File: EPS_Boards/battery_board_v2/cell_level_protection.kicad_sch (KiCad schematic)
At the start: 31 parts

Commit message: eps: battery board: updated schematic
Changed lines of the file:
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@@
     )
   )
-  (global_label "LOW_SIDE_INHIBIT" (shape input) (at 161.29 166.37 180) (fields_autoplaced)
+  (global_label "PACK_N" (shape input) (at 161.29 166.37 180) (fields_autoplaced)
     (effects (font (size 1.27 1.27)) (justify right))
-    (property "Intersheet References" "${INTERSHEET_REFS}" (id 0) (at 142.1855 166.2906 0)
+    (property "Intersheet References" "${INTERSHEET_REFS}" (id 0) (at 151.6802 166.2906 0)
       (effects (font (size 1.27 1.27)) (justify right) hide)
     )
@@
     )
   )
+  (global_label "PACK_P" (shape input) (at 168.91 43.18 270) (fields_autoplaced)
+    (effects (font (size 1.27 1.27)) (justify right))
+    (property "Intersheet References" "${INTERSHEET_REFS}" (id 0) (at 168.9894 52.7293 90)
+      (effects (font (size 1.27 1.27)) (justify right) hide)
+    )
+  )

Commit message: eps: battery board: fixed errors
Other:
- note added: "IV monitor here"
- moved on the sheet: BT?, C?, F?, J?, Q?, R?, U?

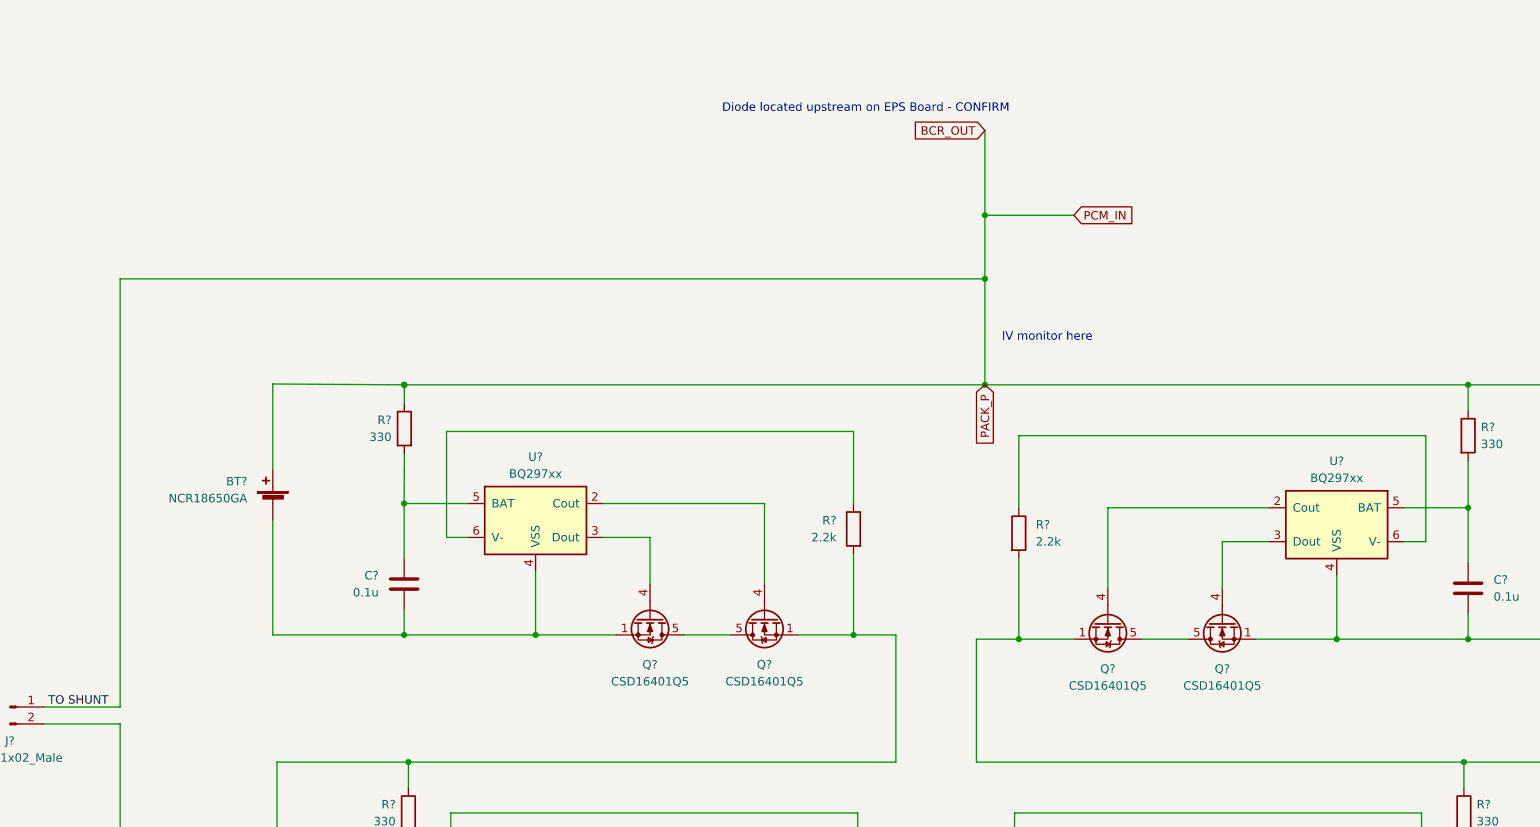
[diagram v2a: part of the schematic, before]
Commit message: eps: battery board: added AND gate for power control and cleaned up global labels
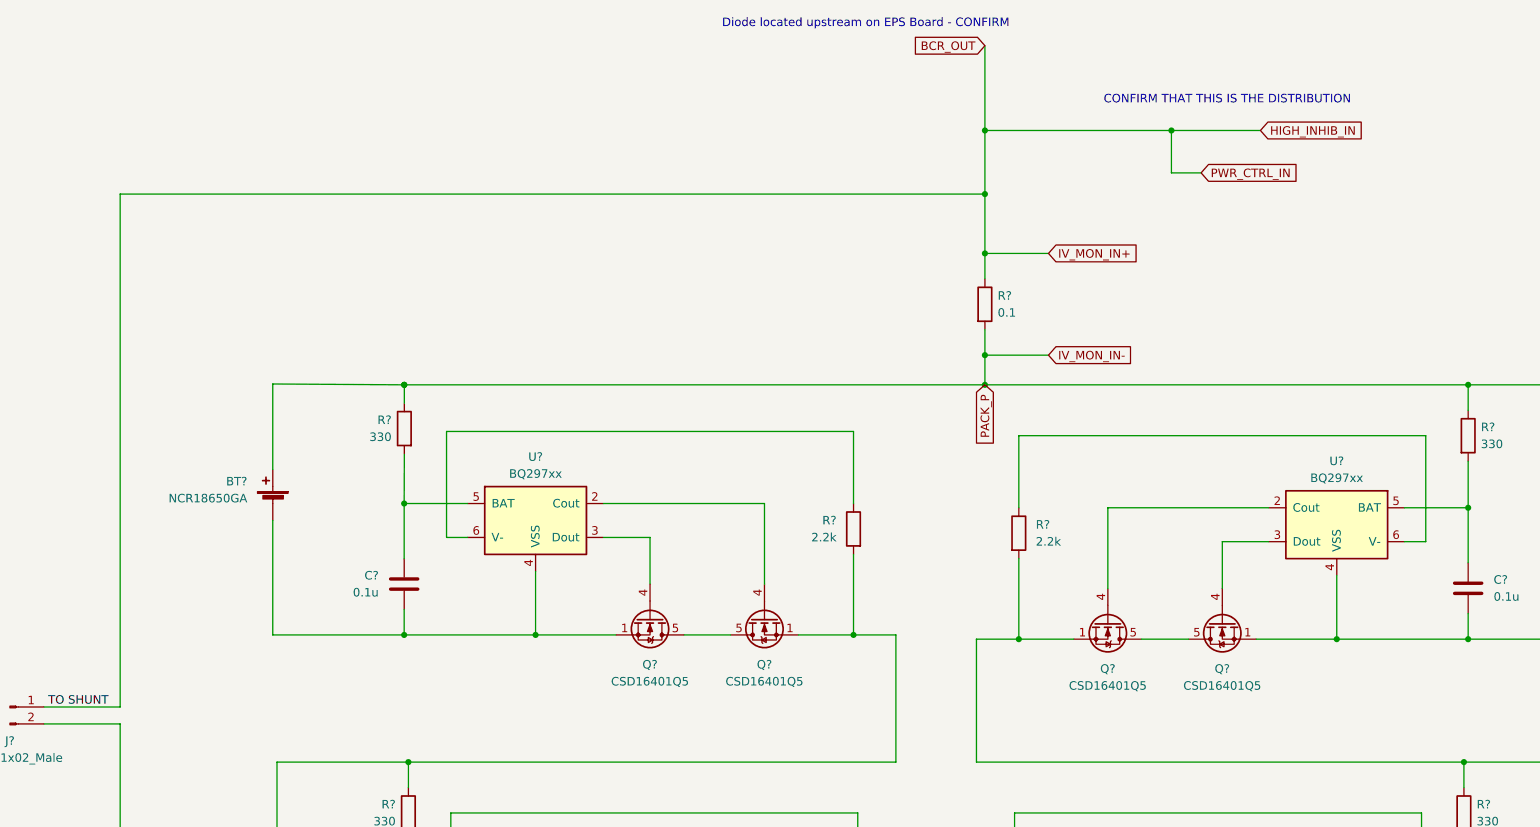
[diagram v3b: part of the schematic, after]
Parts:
- added R?: 0.1, symbol Device:R
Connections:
- net BCR_OUT: now also R?.1; no longer BT?.1 (+), BT?.1 (+), R?.1, R?.1
- new net IV_MON_IN-: BT?.1 (+), BT?.1 (+), R?.1, R?.1, R?.2
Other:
- note added: "CONFIRM THAT THIS IS THE DISTRIBUTION"
- note removed: "IV monitor here"
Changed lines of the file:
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@@
   (junction (at 213.995 187.96) (diameter 0) (color 0 0 0 0)
   )
-  (junction (at 233.045 67.945) (diameter 0) (color 0 0 0 0)
+  (junction (at 233.045 55.245) (diameter 0) (color 0 0 0 0)
   )
   (junction (at 166.37 187.96) (diameter 0) (color 0 0 0 0)
@@
   (junction (at 146.685 149.86) (diameter 0) (color 0 0 0 0)
   )
+  (junction (at 233.045 88.9) (diameter 0) (color 0 0 0 0)
+  )
+  (junction (at 233.045 73.66) (diameter 0) (color 0 0 0 0)
+  )
   (junction (at 146.685 187.96) (diameter 0) (color 0 0 0 0)
   )
@@
   (junction (at 305.435 111.76) (diameter 0) (color 0 0 0 0)
   )
-  (junction (at 233.045 77.47) (diameter 0) (color 0 0 0 0)
+  (junction (at 233.045 64.77) (diameter 0) (color 0 0 0 0)
+  )
+  (junction (at 260.985 55.245) (diameter 0) (color 0 0 0 0)
   )
   (junction (at 146.05 111.125) (diameter 0) (color 0 0 0 0)
@@
     (stroke (width 0) (type default) (color 0 0 0 0))
   )
+  (wire (pts (xy 233.045 85.09) (xy 233.045 88.9))
+    (stroke (width 0) (type default) (color 0 0 0 0))
+  )
   (wire (pts (xy 176.53 168.275) (xy 200.66 168.275))
     (stroke (width 0) (type default) (color 0 0 0 0))
@@
     (stroke (width 0) (type default) (color 0 0 0 0))
   )
-  (wire (pts (xy 103.505 141.605) (xy 103.505 77.47))
+  (wire (pts (xy 103.505 141.605) (xy 103.505 64.77))
+    (stroke (width 0) (type default) (color 0 0 0 0))
+  )
+  (wire (pts (xy 260.985 61.595) (xy 265.43 61.595))
     (stroke (width 0) (type default) (color 0 0 0 0))
   )
@@
     (stroke (width 0) (type default) (color 0 0 0 0))
   )
+  (wire (pts (xy 233.045 73.66) (xy 242.57 73.66))
+    (stroke (width 0) (type default) (color 0 0 0 0))
+  )
   (wire (pts (xy 127 149.86) (xy 146.685 149.86))
     (stroke (width 0) (type default) (color 0 0 0 0))
@@
     (stroke (width 0) (type default) (color 0 0 0 0))
   )
-  (wire (pts (xy 233.045 67.945) (xy 246.38 67.945))
+  (wire (pts (xy 233.045 55.245) (xy 260.985 55.245))
     (stroke (width 0) (type default) (color 0 0 0 0))
   )
@@
     (stroke (width 0) (type default) (color 0 0 0 0))
   )
-  (wire (pts (xy 233.045 77.47) (xy 233.045 93.345))
+  (wire (pts (xy 233.045 64.77) (xy 233.045 73.66))
     (stroke (width 0) (type default) (color 0 0 0 0))
   )
@@
     (stroke (width 0) (type default) (color 0 0 0 0))
   )
+  (wire (pts (xy 233.045 88.9) (xy 242.57 88.9))
+    (stroke (width 0) (type default) (color 0 0 0 0))
+  )
   (wire (pts (xy 183.515 173.355) (xy 183.515 180.34))
     (stroke (width 0) (type default) (color 0 0 0 0))
@@
     (stroke (width 0) (type default) (color 0 0 0 0))
   )
+  (wire (pts (xy 260.985 55.245) (xy 274.32 55.245))
+    (stroke (width 0) (type default) (color 0 0 0 0))
+  )
   (wire (pts (xy 195.58 187.96) (xy 188.595 187.96))
     (stroke (width 0) (type default) (color 0 0 0 0))
@@
     (stroke (width 0) (type default) (color 0 0 0 0))
   )
-  (wire (pts (xy 233.045 67.945) (xy 233.045 77.47))
+  (wire (pts (xy 233.045 55.245) (xy 233.045 64.77))
     (stroke (width 0) (type default) (color 0 0 0 0))
   )
@@
     (stroke (width 0) (type default) (color 0 0 0 0))
   )
+  (wire (pts (xy 233.045 73.66) (xy 233.045 77.47))
+    (stroke (width 0) (type default) (color 0 0 0 0))
+  )
   (wire (pts (xy 325.12 93.345) (xy 325.12 106.68))
     (stroke (width 0) (type default) (color 0 0 0 0))
@@
     (stroke (width 0) (type default) (color 0 0 0 0))
   )
-  (wire (pts (xy 103.505 77.47) (xy 233.045 77.47))
+  (wire (pts (xy 233.045 88.9) (xy 233.045 93.345))
+    (stroke (width 0) (type default) (color 0 0 0 0))
+  )
+  (wire (pts (xy 103.505 64.77) (xy 233.045 64.77))
     (stroke (width 0) (type default) (color 0 0 0 0))
   )
@@
     (stroke (width 0) (type default) (color 0 0 0 0))
   )
+  (wire (pts (xy 260.985 55.245) (xy 260.985 61.595))
+    (stroke (width 0) (type default) (color 0 0 0 0))
+  )
   (wire (pts (xy 304.8 161.29) (xy 304.8 168.275))
     (stroke (width 0) (type default) (color 0 0 0 0))
@@
     (stroke (width 0) (type default) (color 0 0 0 0))
   )
-  (wire (pts (xy 233.045 55.245) (xy 233.045 67.945))
+  (wire (pts (xy 233.045 42.545) (xy 233.045 55.245))
     (stroke (width 0) (type default) (color 0 0 0 0))
   )
@@
     (stroke (width 0) (type default) (color 0 0 0 0))
   )
-  (text "IV monitor here\n" (at 235.585 86.995 0)
+  (text "Diode located upstream on EPS Board - CONFIRM" (at 193.675 40.005 0)
     (effects (font (size 1.27 1.27)) (justify left bottom))
   )
-  (text "Diode located upstream on EPS Board - CONFIRM" (at 193.675 52.705 0)
+  (text "CONFIRM THAT THIS IS THE DISTRIBUTION\n" (at 250.825 51.435 0)
     (effects (font (size 1.27 1.27)) (justify left bottom))
   )
   (label "TO SHUNT" (at 92.71 141.605 0)
     (effects (font (size 1.27 1.27)) (justify left bottom))
+  )
+  (global_label "IV_MON_IN-" (shape input) (at 242.57 88.9 0) (fields_autoplaced)
+    (effects (font (size 1.27 1.27)) (justify left))
+    (property "Intersheet References" "${INTERSHEET_REFS}" (id 0) (at 256.1428 88.8206 0)
+      (effects (font (size 1.27 1.27)) (justify left) hide)
+    )
   )
   (global_label "STAR_GND" (shape input) (at 127 187.96 180) (fields_autoplaced)
@@
     )
   )
-  (global_label "BCR_OUT" (shape input) (at 233.045 55.245 180) (fields_autoplaced)
+  (global_label "BCR_OUT" (shape input) (at 233.045 42.545 180) (fields_autoplaced)
     (effects (font (size 1.27 1.27)) (justify right))
-    (property "Intersheet References" "${INTERSHEET_REFS}" (id 0) (at 222.2257 55.1656 0)
+    (property "Intersheet References" "${INTERSHEET_REFS}" (id 0) (at 222.2257 42.4656 0)
       (effects (font (size 1.27 1.27)) (justify right) hide)
     )
@@
     )
   )
+  (global_label "IV_MON_IN+" (shape input) (at 242.57 73.66 0) (fields_autoplaced)
+    (effects (font (size 1.27 1.27)) (justify left))
+    (property "Intersheet References" "${INTERSHEET_REFS}" (id 0) (at 256.1428 73.5806 0)
+      (effects (font (size 1.27 1.27)) (justify left) hide)
+    )
+  )
   (global_label "STAR_GND" (shape input) (at 324.485 187.9346 0) (fields_autoplaced)
     (effects (font (size 1.27 1.27)) (justify left))
@@
     )
   )
-  (global_label "PCM_IN" (shape input) (at 246.38 67.945 0) (fields_autoplaced)
+  (global_label "PWR_CTRL_IN" (shape input) (at 265.43 61.595 0) (fields_autoplaced)
     (effects (font (size 1.27 1.27)) (justify left))
-    (property "Intersheet References" "${INTERSHEET_REFS}" (id 0) (at 255.6874 67.8656 0)
+    (property "Intersheet References" "${INTERSHEET_REFS}" (id 0) (at 280.1518 61.5156 0)
       (effects (font (size 1.27 1.27)) (justify left) hide)
     )
@@
     (property "Intersheet References" "${INTERSHEET_REFS}" (id 0) (at 233.1244 102.8943 90)
       (effects (font (size 1.27 1.27)) (justify right) hide)
+    )
+  )
+  (global_label "HIGH_INHIB_IN" (shape input) (at 274.32 55.245 0) (fields_autoplaced)
+    (effects (font (size 1.27 1.27)) (justify left))
+    (property "Intersheet References" "${INTERSHEET_REFS}" (id 0) (at 290.1909 55.1656 0)
+      (effects (font (size 1.27 1.27)) (justify left) hide)
     )
   )
@@
       (effects (font (size 1.27 1.27)) hide)
     )
+    (pin "1")
+    (pin "2")
+  )
+  (symbol (lib_id "Device:R") (at 233.045 81.28 0) (unit 1)
+    (in_bom yes) (on_board yes) (fields_autoplaced)
+    (property "Reference" "R?" (id 0) (at 234.95 80.0099 0)
+      (effects (font (size 1.27 1.27)) (justify left))
+    )
+    (property "Value" "0.1" (id 1) (at 234.95 82.5499 0)
+      (effects (font (size 1.27 1.27)) (justify left))
+    )
+    (property "Footprint" "" (id 2) (at 231.267 81.28 90)
+      (effects (font (size 1.27 1.27)) hide)
+    )
+    (property "Datasheet" "~" (id 3) (at 233.045 81.28 0)
+      (effects (font (size 1.27 1.27)) hide)
+    )

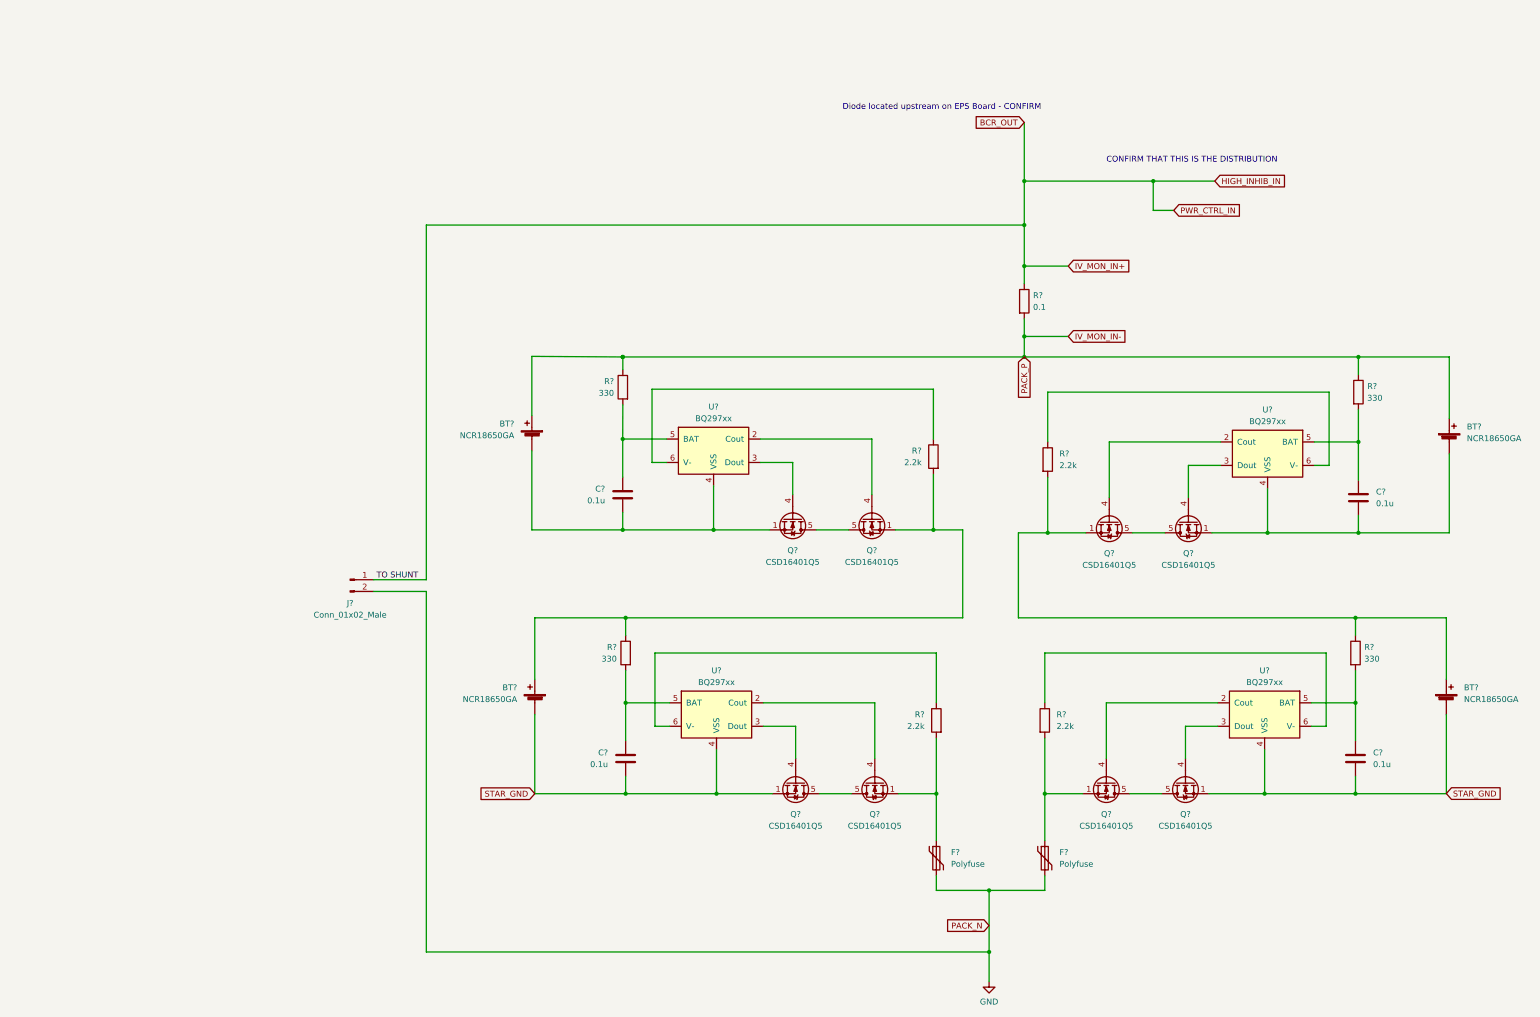
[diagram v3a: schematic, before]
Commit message: eps: battery board: finializing schematic
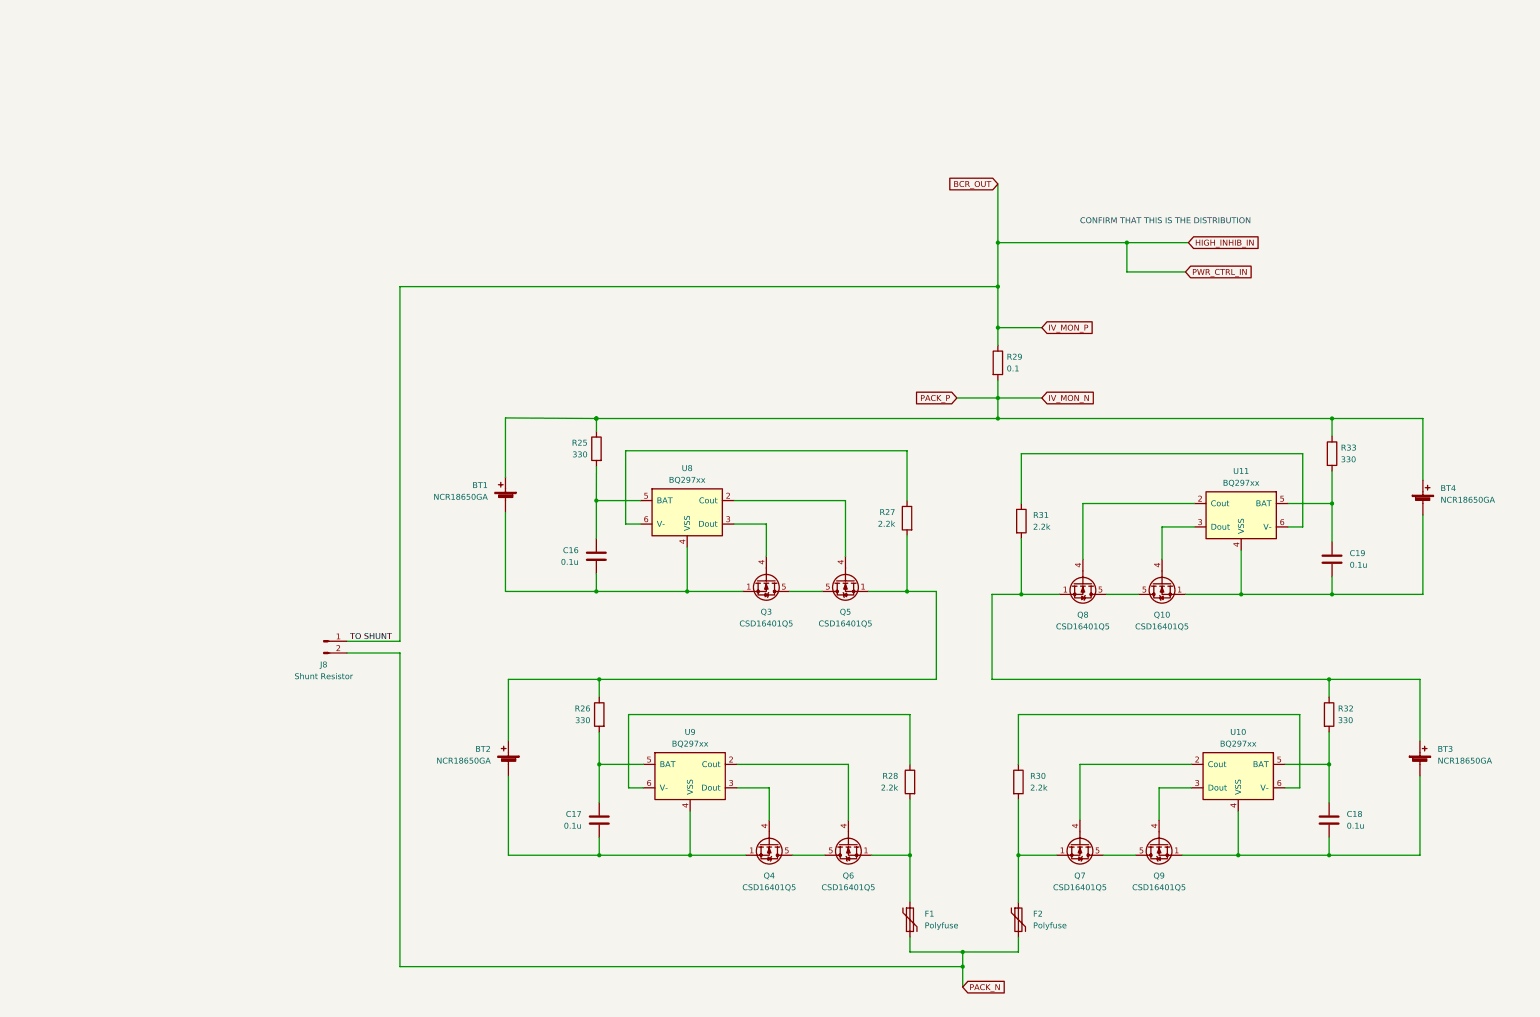
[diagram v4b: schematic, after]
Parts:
- BT1, BT2, BT3, BT4: renamed from BT?; footprint (none) -> qset-footprints:Keystone_54_18650
- J8: renamed from J?; value Conn_01x02_Male -> Shunt Resistor; footprint (none) -> Connector_PinHeader_2.00mm:PinHeader_1x02_P2.00mm_Vertical
- gave numbers to parts that had none: 27
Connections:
- net GND renamed PACK_N
- net IV_MON_IN- renamed IV_MON_N
- net STAR_GND: no longer names the net of BT2.2 (-), C17.1, Q4.1 (S), Q4.2 (S), Q4.3 (S), U9.4 (VSS)
- net STAR_GND: no longer BT3.2 (-), C18.1, Q9.1 (S), Q9.2 (S), Q9.3 (S), U10.4 (VSS)
- new net: BT3.2 (-), C18.1, Q9.1 (S), Q9.2 (S), Q9.3 (S), U10.4 (VSS)
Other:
- note removed: "Diode located upstream on EPS Board - CONFIRM"
- moved on the sheet: BT1, BT2, BT3, BT4, C16, C17, C18, C19, F1, F2, J8, Q10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
